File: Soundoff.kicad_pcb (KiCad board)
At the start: 4 copper layers, 27.4 x 19.3 mm, 29 parts, among them J1 Debug, J2 USB-C Receptacle, P1 Switched USB-C, U1 3.3V LDO, U16 TLP3123, U2 CH334F, U3 EMS4000RSW, U4 STM32F042G6Ux, Y1 12 MHz, 20pF

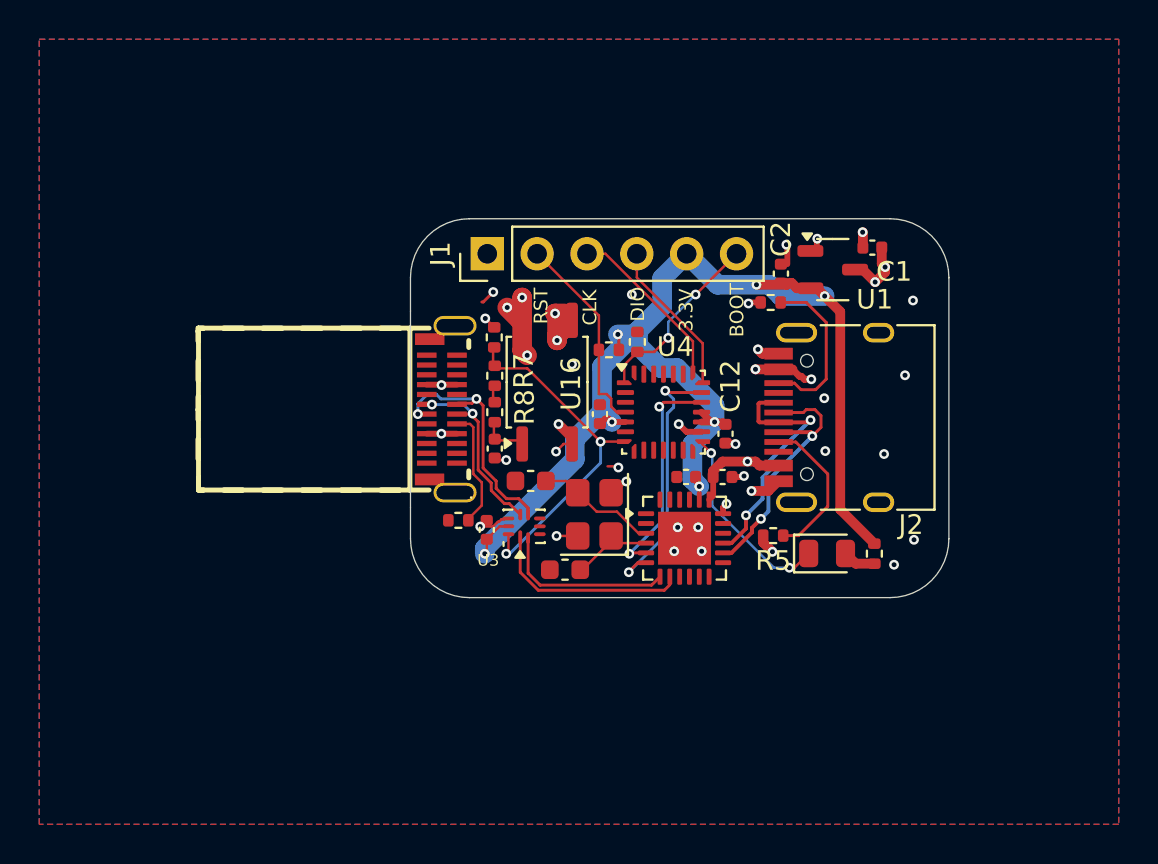
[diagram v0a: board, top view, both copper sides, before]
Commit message: v3: fix usb polarity
The USB polarity was incorrect -- the DFP and UFP roles were swapped.
Change the connectors around to make it correct now.

Signed-off-by: Sean Cross <sean@xobs.io>
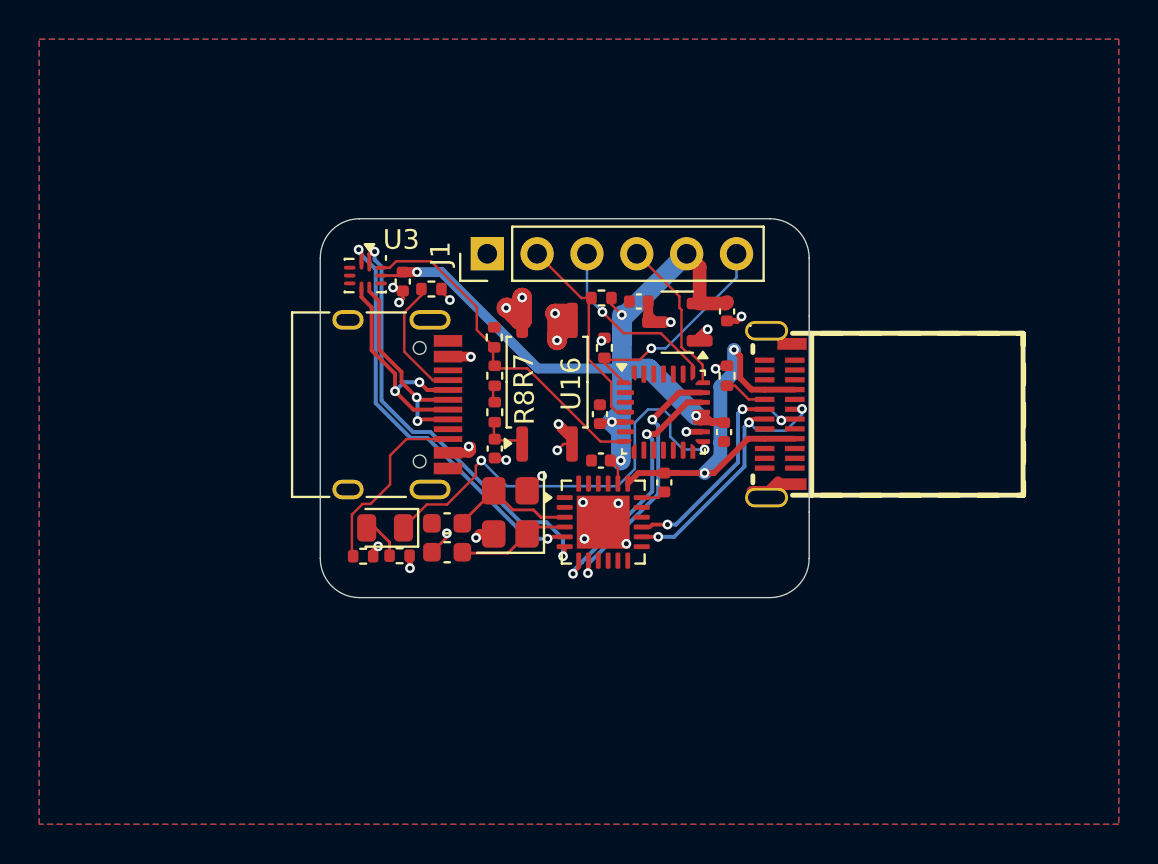
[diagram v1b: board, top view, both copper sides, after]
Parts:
- removed R6: R 5.1k 0402, Resistor_SMD:R_0402_1005Metric
- added R10: R 5.1k 0402, Resistor_SMD:R_0402_1005Metric, F.Cu at (106.5, 61.3)
- moved J2 24.9 mm to (106.8, 53.6), turned to -90 degrees
- moved R1 24.2 mm to (108.4, 61.3), turned to 180 degrees
- moved D1 22.6 mm to (107.6, 59.9), turned to 180 degrees
- moved P1 17.2 mm to (127.7, 54.1), turned to 90 degrees
- moved U3 15.1 mm to (106.6, 47.0), turned to -90 degrees
- moved C15 13.4 mm to (108.5, 47.3), turned to -90 degrees
- moved C1 12.2 mm to (120.5, 48.4)
- moved R9 11.9 mm to (110.0, 47.7), turned to 0 degrees
- moved R5 8.48 mm to (125.0, 52.1), turned to -90 degrees
- moved U1 8.36 mm to (122.5, 49.4), turned to 180 degrees
- moved C4 6.07 mm to (110.8, 61.1)
- moved C5 4.77 mm to (110.8, 59.7)
- moved C14 4.42 mm to (118.6, 56.5)
- moved Y1 4.28 mm to (114.0, 59.1)
- moved U2 4.22 mm to (118.7, 59.6)
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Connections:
- J2 pad A4: VUSB -> VUSB_SW
- J2 pad A6: /UFP_USB_D+ -> /TGT_SW_USB_D+
- J2 pad A7: /UFP_USB_D- -> /TGT_SW_USB_D-
- J2 pad A9: VUSB -> VUSB_SW
- J2 pad B4: VUSB -> VUSB_SW
- J2 pad B6: /UFP_USB_D+ -> /TGT_SW_USB_D+
- J2 pad B7: /UFP_USB_D- -> /TGT_SW_USB_D-
- J2 pad B9: VUSB -> VUSB_SW
- P1 pad A4: VUSB_SW -> VUSB
- P1 pad A6: /TGT_SW_USB_D+ -> /UFP_USB_D+
- P1 pad A7: /TGT_SW_USB_D- -> /UFP_USB_D-
- P1 pad A9: VUSB_SW -> VUSB
- P1 pad B4: VUSB_SW -> VUSB
- P1 pad B6: /TGT_SW_USB_D+ -> /UFP_USB_D+
- P1 pad B7: /TGT_SW_USB_D- -> /UFP_USB_D-
- P1 pad B9: VUSB_SW -> VUSB
- R5 pad 2: Net-(J2-CC1) -> Net-(P1-CC)
- R9 pad 1: Net-(P1-CC) -> Net-(J2-CC1)
- U2 pad 5: /DBG_USB_D- -> /TGT_USB_D-
- U2 pad 6: /DBG_USB_D+ -> /TGT_USB_D+
- U2 pad 7: /TGT_USB_D- -> /DBG_USB_D-
- U2 pad 8: /TGT_USB_D+ -> /DBG_USB_D+
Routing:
- net VUSB: track 15.2 -> 40.4 mm, vias 8 -> 5
- net /TGT_USB_D-: track 8.94 -> 21.5 mm, vias 0 -> 2
- net Net-(D1-K): track 10.0 -> 22.5 mm
- net /TGT_USB_D+: track 10.3 -> 22.2 mm, vias 0 -> 2
- net VUSB_SW: track 21.9 -> 16.8 mm
- net 3.3V: track 65.7 -> 61.6 mm, vias 7 -> 6
- net Net-(P1-CC): track 6.03 -> 2.20 mm
- net GND: track 18.2 -> 15.6 mm, vias 33 -> 19
- net /BOOT0: track 9.45 -> 11.3 mm, vias 2 -> 1
- net /DBG_USB_D-: track 11.4 -> 13.1 mm
- net Net-(U2-XI): track 3.48 -> 5.22 mm
- net /TGT_SW_USB_D+: track 9.26 -> 10.9 mm
- net Net-(J2-CC1): track 7.72 -> 6.38 mm
- net Net-(J2-CC2): track 8.42 -> 9.41 mm
- net /UFP_USB_D+: track 13.0 -> 13.6 mm, vias 2 -> 3
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- added copper zone on In2.Cu, net GND
- removed copper zone on In2.Cu, net VUSB
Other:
- board size 27.4 x 19.3 mm -> 24.9 x 19.3 mm
- board text added: "Soundoff V3 02/06/2026 Designed in HK"
- board text removed: "3.3V"
- board text removed: "BOOT"
- board text removed: "CLK"
- board text removed: "DIO"
- board text removed: "RST"
- board text removed: "Soundoff V2 01/06/2026 Designed in HK"
